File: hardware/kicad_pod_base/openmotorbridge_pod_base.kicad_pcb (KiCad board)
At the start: 2 copper layers, 24 x 14 mm, 6 parts

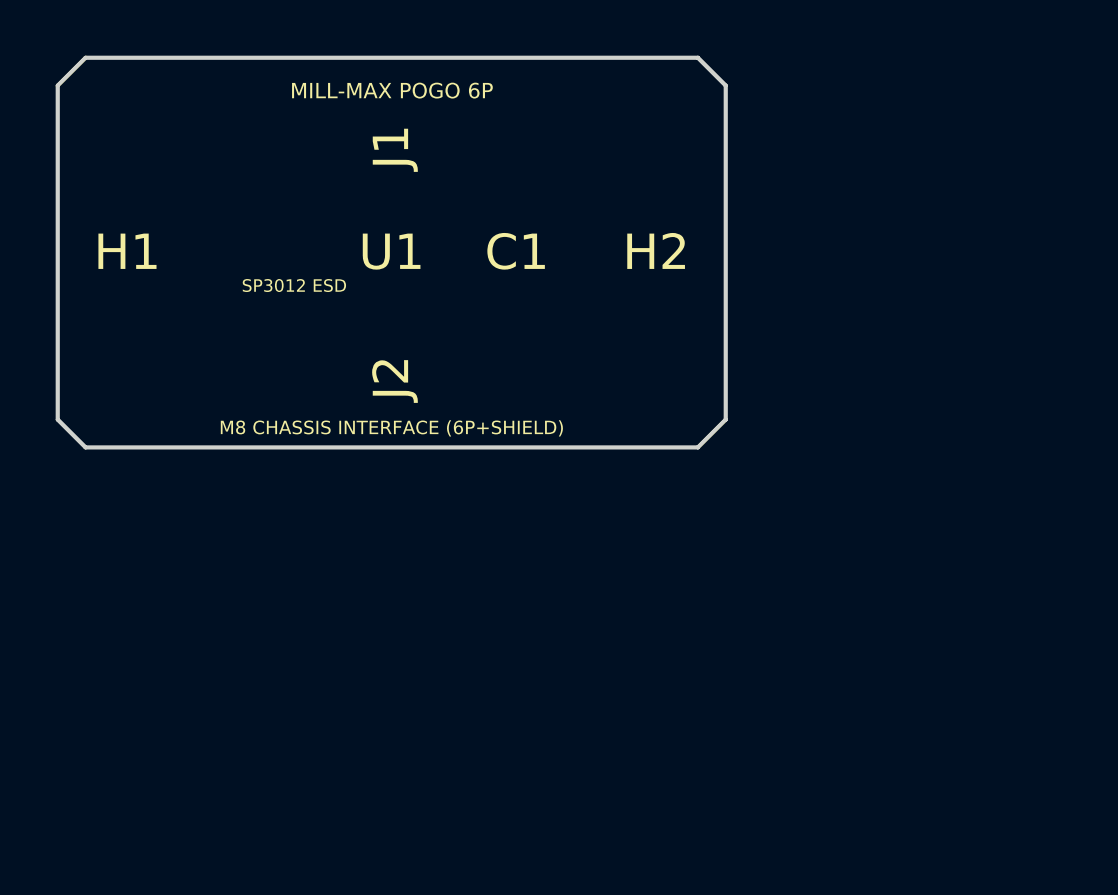
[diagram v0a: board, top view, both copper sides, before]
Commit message: feat(hardware): finalize direct PCB-mount M8 receptacle on pod base with 28x28mm layout and generous clearances
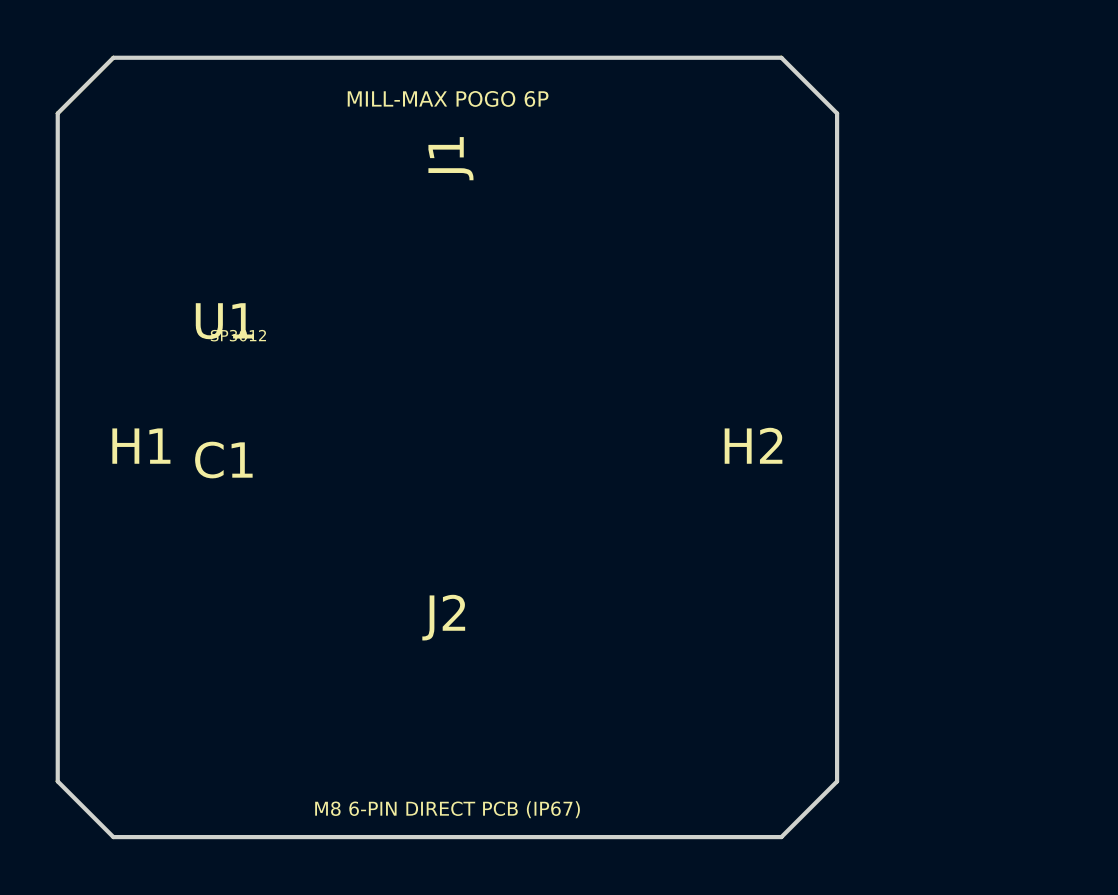
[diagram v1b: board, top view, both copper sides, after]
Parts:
- moved C1 12.9 mm to (106.0, 84.5)
- moved J2 8.73 mm to (114.0, 90.0), turned to 0 degrees
- moved H2 7.83 mm to (125.0, 84.0)
- moved H1 7.02 mm to (103.0, 84.0)
- moved U1 6.50 mm to (106.0, 79.5)
- moved J1 2.02 mm to (114.0, 73.5)
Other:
- board size 24 x 14 mm -> 28 x 28 mm
- board text added: "M8 6-PIN DIRECT PCB (IP67)"
- board text added: "SP3012"
- board text removed: "M8 CHASSIS INTERFACE (6P+SHIELD)"
- board text removed: "SP3012 ESD"

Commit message: feat(cad/mech): implement Stirnwand-Adapter (End-Cap) Pod & horizontal cartridge insertion architecture
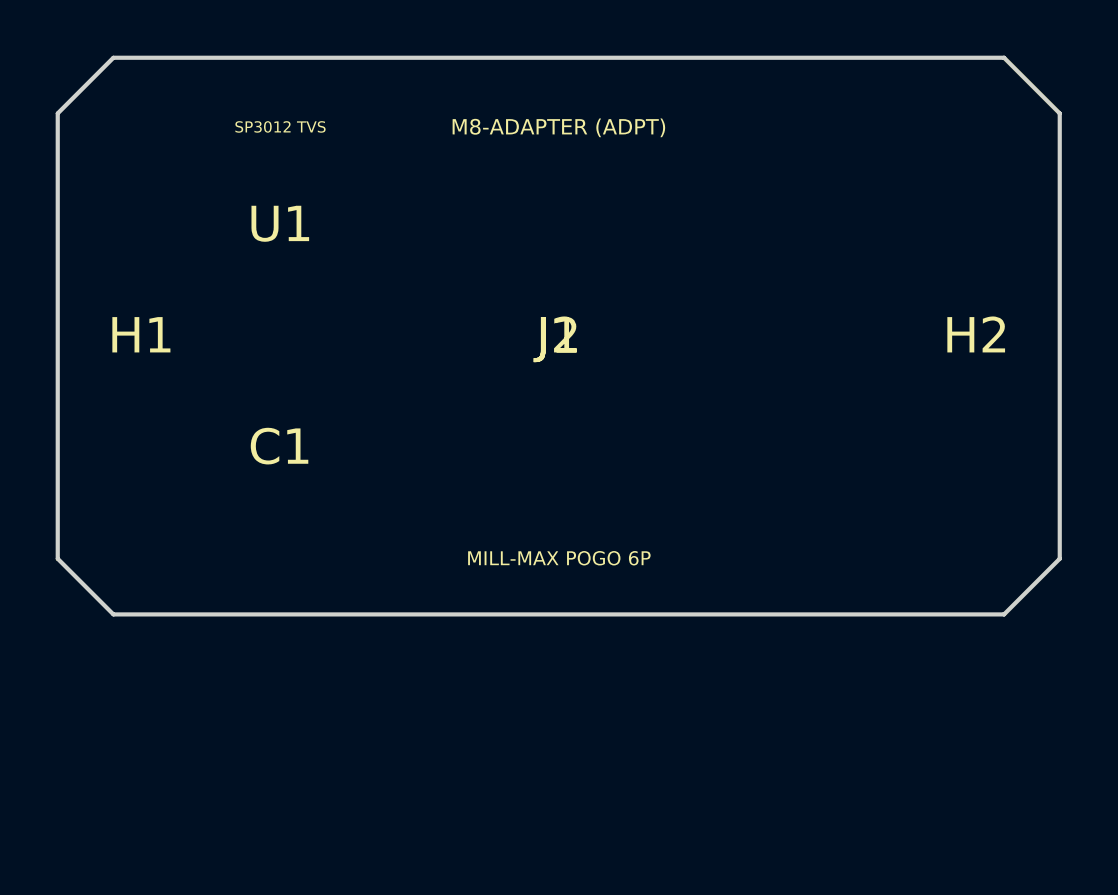
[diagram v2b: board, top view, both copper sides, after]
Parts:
- moved J2 10.8 mm to (118.0, 80.0)
- moved H2 8.94 mm to (133.0, 80.0)
- moved J1 7.63 mm to (118.0, 80.0), turned to 0 degrees
- moved U1 4.03 mm to (108.0, 76.0)
- moved H1 4.00 mm to (103.0, 80.0)
- moved C1 2.06 mm to (108.0, 84.0)
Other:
- board size 28 x 28 mm -> 36 x 20 mm
- board text added: "M8-ADAPTER (ADPT)"
- board text added: "SP3012 TVS"
- board text removed: "M8 6-PIN DIRECT PCB (IP67)"
- board text removed: "SP3012"
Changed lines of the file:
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@@
 	(footprint ""
 		(layer "F.Cu")
-		(at 103 84)
-		(property "Reference" "H1"
-			(at 0 0 0)
-			(layer "F.SilkS")
-			(effects
-				(font
-					(size 1.27 1.27)
-				)
-			)
-		)
-		(property "Value" ""
-			(at 0 0 0)
-			(layer "F.Fab")
-			(effects
-				(font
-					(size 1.27 1.27)
-				)
-			)
-		)
-		(property "Datasheet" ""
-			(at 0 0 0)
-			(layer "F.Fab")
-			(hide yes)
-			(effects
-				(font
-					(size 1.27 1.27)
-				)
-			)
-		)
-		(property "Description" ""
-			(at 0 0 0)
-			(layer "F.Fab")
-			(hide yes)
-			(effects
-				(font
-					(size 1.27 1.27)
-				)
-			)
-		)
-		(duplicate_pad_numbers_are_jumpers no)
-		(embedded_fonts no)
-	)
-	(footprint ""
-		(layer "F.Cu")
-		(at 106 79.5)
+		(at 108 76)
 		(property "Reference" "U1"
 			(at 0 0 0)
@@
 	(footprint ""
 		(layer "F.Cu")
-		(at 114 90)
+		(at 103 80)
+		(property "Reference" "H1"
+			(at 0 0 0)
+			(layer "F.SilkS")
+			(effects
+				(font
+					(size 1.27 1.27)
+				)
+			)
+		)
+		(property "Value" ""
+			(at 0 0 0)
+			(layer "F.Fab")
+			(effects
+				(font
+					(size 1.27 1.27)
+				)
+			)
+		)
+		(property "Datasheet" ""
+			(at 0 0 0)
+			(layer "F.Fab")
+			(hide yes)
+			(effects
+				(font
+					(size 1.27 1.27)
+				)
+			)
+		)
+		(property "Description" ""
+			(at 0 0 0)
+			(layer "F.Fab")
+			(hide yes)
+			(effects
+				(font
+					(size 1.27 1.27)
+				)
+			)
+		)
+		(duplicate_pad_numbers_are_jumpers no)
+		(embedded_fonts no)
+	)
+	(footprint ""
+		(layer "F.Cu")
+		(at 108 84)
+		(property "Reference" "C1"
+			(at 0 0 0)
+			(layer "F.SilkS")
+			(effects
+				(font
+					(size 1.27 1.27)
+				)
+			)
+		)
+		(property "Value" ""
+			(at 0 0 0)
+			(layer "F.Fab")
+			(effects
+				(font
+					(size 1.27 1.27)
+				)
+			)
+		)
+		(property "Datasheet" ""
+			(at 0 0 0)
+			(layer "F.Fab")
+			(hide yes)
+			(effects
+				(font
+					(size 1.27 1.27)
+				)
+			)
+		)
+		(property "Description" ""
+			(at 0 0 0)
+			(layer "F.Fab")
+			(hide yes)
+			(effects
+				(font
+					(size 1.27 1.27)
+				)
+			)
+		)
+		(duplicate_pad_numbers_are_jumpers no)
+		(embedded_fonts no)
+		(model "${KICAD10_3DMODEL_DIR}/Capacitor_SMD.3dshapes/C_0603_1608Metric.step"
+			(offset
+				(xyz 0 0 0)
+			)
+			(scale
+				(xyz 1 1 1)
+			)
+			(rotate
+				(xyz 0 0 0)
+			)
+		)
+	)
+	(footprint ""
+		(layer "F.Cu")
+		(at 118 80)
 		(property "Reference" "J2"
 			(at 0 0 0)
@@
 	(footprint ""
 		(layer "F.Cu")
-		(at 114 73.5 90)
+		(at 118 80)
 		(property "Reference" "J1"
-			(at 0 0 90)
-			(layer "F.SilkS")
-			(effects
-				(font
-					(size 1.27 1.27)
-				)
-			)
-		)
-		(property "Value" ""
-			(at 0 0 90)
-			(layer "F.Fab")
-			(effects
-				(font
-					(size 1.27 1.27)
-				)
-			)
-		)
-		(property "Datasheet" ""
-			(at 0 0 90)
-			(layer "F.Fab")
-			(hide yes)
-			(effects
-				(font
-					(size 1.27 1.27)
-				)
-			)
-		)
-		(property "Description" ""
-			(at 0 0 90)
+			(at 0 0 0)
+			(layer "F.SilkS")
+			(effects
+				(font
+					(size 1.27 1.27)
+				)
+			)
+		)
+		(property "Value" ""
+			(at 0 0 0)
+			(layer "F.Fab")
+			(effects
+				(font
+					(size 1.27 1.27)
+				)
+			)
+		)
+		(property "Datasheet" ""
+			(at 0 0 0)
+			(layer "F.Fab")
+			(hide yes)
+			(effects
+				(font
+					(size 1.27 1.27)
+				)
+			)
+		)
+		(property "Description" ""
+			(at 0 0 0)
 			(layer "F.Fab")
 			(hide yes)
@@
 	(footprint ""
 		(layer "F.Cu")
-		(at 106 84.5)
-		(property "Reference" "C1"
-			(at 0 0 0)
-			(layer "F.SilkS")
-			(effects
-				(font
-					(size 1.27 1.27)
-				)
-			)
-		)
-		(property "Value" ""
-			(at 0 0 0)
-			(layer "F.Fab")
-			(effects
-				(font
-					(size 1.27 1.27)
-				)
-			)
-		)
-		(property "Datasheet" ""
-			(at 0 0 0)
-			(layer "F.Fab")
-			(hide yes)
-			(effects
-				(font
-					(size 1.27 1.27)
-				)
-			)
-		)
-		(property "Description" ""
-			(at 0 0 0)
-			(layer "F.Fab")
-			(hide yes)
-			(effects
-				(font
-					(size 1.27 1.27)
-				)
-			)
-		)
-		(duplicate_pad_numbers_are_jumpers no)
-		(embedded_fonts no)
-		(model "${KICAD10_3DMODEL_DIR}/Capacitor_SMD.3dshapes/C_0603_1608Metric.step"
-			(offset
-				(xyz 0 0 0)
-			)
-			(scale
-				(xyz 1 1 1)
-			)
-			(rotate
-				(xyz 0 0 0)
-			)
-		)
-	)
-	(footprint ""
-		(layer "F.Cu")
-		(at 125 84)
+		(at 133 80)
 		(property "Reference" "H2"
 			(at 0 0 0)
@@
 	)
 	(gr_line
-		(start 100 96)
+		(start 100 88)
 		(end 100 72)
 		(stroke
@@
 	(gr_line
 		(start 102 70)
-		(end 126 70)
-		(stroke
-			(width 0.15)
-			(type default)
-		)
-		(layer "Edge.Cuts")
-	)
-	(gr_line
-		(start 102 98)
-		(end 100 96)
-		(stroke
-			(width 0.15)
-			(type default)
-		)
-		(layer "Edge.Cuts")
-	)
-	(gr_line
-		(start 126 70)
-		(end 128 72)
-		(stroke
-			(width 0.15)
-			(type default)
-		)
-		(layer "Edge.Cuts")
-	)
-	(gr_line
-		(start 126 98)
-		(end 102 98)
-		(stroke
-			(width 0.15)
-			(type default)
-		)
-		(layer "Edge.Cuts")
-	)
-	(gr_line
-		(start 128 72)
-		(end 128 96)
-		(stroke
-			(width 0.15)
-			(type default)
-		)
-		(layer "Edge.Cuts")
-	)
-	(gr_line
-		(start 128 96)
-		(end 126 98)
-		(stroke
-			(width 0.15)
-			(type default)
-		)
-		(layer "Edge.Cuts")
-	)
-	(gr_text "SP3012"
-		(at 106.5 80 0)
+		(end 134 70)
+		(stroke
+			(width 0.15)
+			(type default)
+		)
+		(layer "Edge.Cuts")
+	)
+	(gr_line
+		(start 102 90)
+		(end 100 88)
+		(stroke
+			(width 0.15)
+			(type default)
+		)
+		(layer "Edge.Cuts")
+	)
+	(gr_line
+		(start 134 70)
+		(end 136 72)
+		(stroke
+			(width 0.15)
+			(type default)
+		)
+		(layer "Edge.Cuts")
+	)
+	(gr_line
+		(start 134 90)
+		(end 102 90)
+		(stroke
+			(width 0.15)
+			(type default)
+		)
+		(layer "Edge.Cuts")
+	)
+	(gr_line
+		(start 136 72)
+		(end 136 88)
+		(stroke
+			(width 0.15)
+			(type default)
+		)
+		(layer "Edge.Cuts")
+	)
+	(gr_line
+		(start 136 88)
+		(end 134 90)
+		(stroke
+			(width 0.15)
+			(type default)
+		)
+		(layer "Edge.Cuts")
+	)
+	(gr_text "SP3012 TVS"
+		(at 108 72.5 0)
 		(layer "F.SilkS")
 		(effects
@@
 		)
 	)
-	(gr_text "M8 6-PIN DIRECT PCB (IP67)"
-		(at 114 97 0)
+	(gr_text "MILL-MAX POGO 6P"
+		(at 118 88 0)
 		(layer "F.SilkS")
 		(effects
@@
 		)
 	)
-	(gr_text "MILL-MAX POGO 6P"
-		(at 114 71.5 0)
+	(gr_text "M8-ADAPTER (ADPT)"
+		(at 118 72.5 0)
 		(layer "F.SilkS")
 		(effects

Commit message: feat(hardware): center vertical M8 connector on bottom B.Cu and Pogo pins on top F.Cu of pod base PCB
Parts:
- J2: moved to B.Cu
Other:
- board text added: "GND SHIELD PLANE"
- board text added: "M8 6-PIN IP67 (OUTSIDE)"
- board text added: "MILL-MAX POGO 6P (INSIDE)"
- board text added: "OPENMOTORBRIDGE"
- board text removed: "M8-ADAPTER (ADPT)"
- board text removed: "MILL-MAX POGO 6P"
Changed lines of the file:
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@@
+	(footprint ""
+		(layer "F.Cu")
+		(at 103 80)
+		(property "Reference" "H1"
+			(at 0 0 0)
+			(layer "F.SilkS")
+			(effects
+				(font
+					(size 1.27 1.27)
+				)
+			)
+		)
+		(property "Value" ""
+			(at 0 0 0)
+			(layer "F.Fab")
+			(effects
+				(font
+					(size 1.27 1.27)
+				)
+			)
+		)
+		(property "Datasheet" ""
+			(at 0 0 0)
+			(layer "F.Fab")
+			(hide yes)
+			(effects
+				(font
+					(size 1.27 1.27)
+				)
+			)
+		)
+		(property "Description" ""
+			(at 0 0 0)
+			(layer "F.Fab")
+			(hide yes)
+			(effects
+				(font
+					(size 1.27 1.27)
+				)
+			)
+		)
+		(duplicate_pad_numbers_are_jumpers no)
+		(embedded_fonts no)
+	)
+	(footprint ""
+		(layer "F.Cu")
+		(at 133 80)
+		(property "Reference" "H2"
+			(at 0 0 0)
+			(layer "F.SilkS")
+			(effects
+				(font
+					(size 1.27 1.27)
+				)
+			)
+		)
+		(property "Value" ""
+			(at 0 0 0)
+			(layer "F.Fab")
+			(effects
+				(font
+					(size 1.27 1.27)
+				)
+			)
+		)
+		(property "Datasheet" ""
+			(at 0 0 0)
+			(layer "F.Fab")
+			(hide yes)
+			(effects
+				(font
+					(size 1.27 1.27)
+				)
+			)
+		)
+		(property "Description" ""
+			(at 0 0 0)
+			(layer "F.Fab")
+			(hide yes)
+			(effects
+				(font
+					(size 1.27 1.27)
+				)
+			)
+		)
+		(duplicate_pad_numbers_are_jumpers no)
+		(embedded_fonts no)
+	)
 	(footprint ""
 		(layer "F.Cu")
@@
 	(footprint ""
 		(layer "F.Cu")
-		(at 103 80)
-		(property "Reference" "H1"
-			(at 0 0 0)
-			(layer "F.SilkS")
-			(effects
-				(font
-					(size 1.27 1.27)
-				)
-			)
-		)
-		(property "Value" ""
-			(at 0 0 0)
-			(layer "F.Fab")
-			(effects
-				(font
-					(size 1.27 1.27)
-				)
-			)
-		)
-		(property "Datasheet" ""
-			(at 0 0 0)
-			(layer "F.Fab")
-			(hide yes)
-			(effects
-				(font
-					(size 1.27 1.27)
-				)
-			)
-		)
-		(property "Description" ""
-			(at 0 0 0)
-			(layer "F.Fab")
-			(hide yes)
-			(effects
-				(font
-					(size 1.27 1.27)
-				)
-			)
-		)
-		(duplicate_pad_numbers_are_jumpers no)
-		(embedded_fonts no)
-	)
-	(footprint ""
-		(layer "F.Cu")
 		(at 108 84)
 		(property "Reference" "C1"
@@
 			(rotate
 				(xyz 0 0 0)
-			)
-		)
-	)
-	(footprint ""
-		(layer "F.Cu")
-		(at 118 80)
-		(property "Reference" "J2"
-			(at 0 0 0)
-			(layer "F.SilkS")
-			(effects
-				(font
-					(size 1.27 1.27)
-				)
-			)
-		)
-		(property "Value" ""
-			(at 0 0 0)
-			(layer "F.Fab")
-			(effects
-				(font
-					(size 1.27 1.27)
-				)
-			)
-		)
-		(property "Datasheet" ""
-			(at 0 0 0)
-			(layer "F.Fab")
-			(hide yes)
-			(effects
-				(font
-					(size 1.27 1.27)
-				)
-			)
-		)
-		(property "Description" ""
-			(at 0 0 0)
-			(layer "F.Fab")
-			(hide yes)
-			(effects
-				(font
-					(size 1.27 1.27)
-				)
-			)
-		)
-		(duplicate_pad_numbers_are_jumpers no)
-		(embedded_fonts no)
-		(model "${KICAD10_3DMODEL_DIR}/Connector_Audio.3dshapes/Jack_3.5mm_Ledino_KB3SPRS_Horizontal.step"
-			(offset
-				(xyz 4 -1 0)
-			)
-			(scale
-				(xyz 1 1 1)
-			)
-			(rotate
-				(xyz 0 0 -90)
 			)
 		)
@@
 	)
 	(footprint ""
-		(layer "F.Cu")
-		(at 133 80)
-		(property "Reference" "H2"
-			(at 0 0 0)
-			(layer "F.SilkS")
-			(effects
-				(font
-					(size 1.27 1.27)
-				)
-			)
-		)
-		(property "Value" ""
-			(at 0 0 0)
-			(layer "F.Fab")
-			(effects
-				(font
-					(size 1.27 1.27)
-				)
-			)
-		)
-		(property "Datasheet" ""
-			(at 0 0 0)
-			(layer "F.Fab")
-			(hide yes)
-			(effects
-				(font
-					(size 1.27 1.27)
-				)
-			)
-		)
-		(property "Description" ""
-			(at 0 0 0)
-			(layer "F.Fab")
-			(hide yes)
-			(effects
-				(font
-					(size 1.27 1.27)
-				)
-			)
-		)
-		(duplicate_pad_numbers_are_jumpers no)
-		(embedded_fonts no)
+		(layer "B.Cu")
+		(at 118 80)
+		(property "Reference" "J2"
+			(at 0 0 0)
+			(layer "F.SilkS")
+			(effects
+				(font
+					(size 1.27 1.27)
+				)
+			)
+		)
+		(property "Value" ""
+			(at 0 0 0)
+			(layer "F.Fab")
+			(effects
+				(font
+					(size 1.27 1.27)
+				)
+			)
+		)
+		(property "Datasheet" ""
+			(at 0 0 0)
+			(layer "F.Fab")
+			(hide yes)
+			(effects
+				(font
+					(size 1.27 1.27)
+				)
+			)
+		)
+		(property "Description" ""
+			(at 0 0 0)
+			(layer "F.Fab")
+			(hide yes)
+			(effects
+				(font
+					(size 1.27 1.27)
+				)
+			)
+		)
+		(duplicate_pad_numbers_are_jumpers no)
+		(embedded_fonts no)
+		(model "${KICAD10_3DMODEL_DIR}/Connector_Coaxial.3dshapes/SMA_Amphenol_132291_Vertical.step"
+			(offset
+				(xyz 0 0 0)
+			)
+			(scale
+				(xyz 1.3 1.3 1.3)
+			)
+			(rotate
+				(xyz 0 0 0)
+			)
+		)
 	)
 	(gr_line
@@
 	)
 	(gr_text "SP3012 TVS"
-		(at 108 72.5 0)
+		(at 108 72.2 0)
 		(layer "F.SilkS")
 		(effects
 			(font
-				(size 0.4 0.4)
+				(size 0.45 0.45)
 				(thickness 0.1)
 			)
 		)
 	)
-	(gr_text "MILL-MAX POGO 6P"
-		(at 118 88 0)
+	(gr_text "MILL-MAX POGO 6P (INSIDE)"
+		(at 118 87.8 0)
 		(layer "F.SilkS")
 		(effects
@@
 		)
 	)
-	(gr_text "M8-ADAPTER (ADPT)"
-		(at 118 72.5 0)
+	(gr_text "OPENMOTORBRIDGE"
+		(at 118 72.2 0)
 		(layer "F.SilkS")
 		(effects
 			(font
+				(size 0.6 0.6)
+				(thickness 0.12)
+			)
+		)
+	)
+	(gr_text "GND SHIELD PLANE"
+		(at 118 87.5 0)
+		(layer "B.SilkS")
+		(effects
+			(font
+				(size 0.45 0.45)
+				(thickness 0.1)
+			)
+		)
+	)
+	(gr_text "M8 6-PIN IP67 (OUTSIDE)"
+		(at 118 72.5 0)
+		(layer "B.SilkS")
+		(effects
+			(font
